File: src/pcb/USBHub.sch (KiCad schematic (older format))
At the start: 3 parts

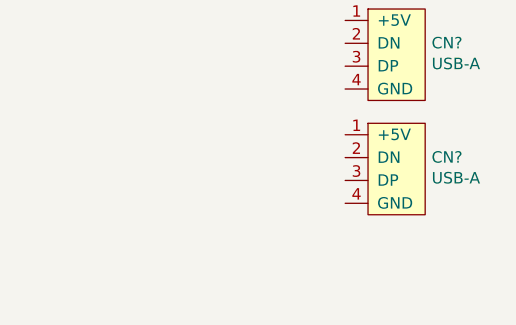
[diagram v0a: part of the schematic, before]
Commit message: added more connections, clarified schematic. Also added missing schematics
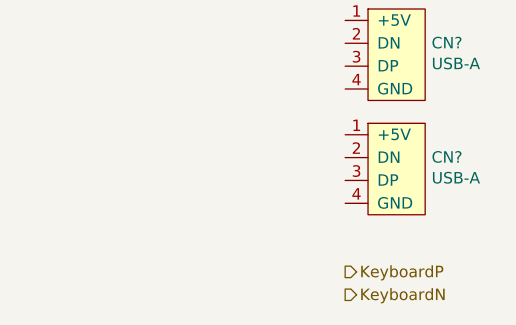
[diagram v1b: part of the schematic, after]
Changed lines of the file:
@@
 Text HLabel 7500 3500 2    50   Output ~ 0
 MCUUSBN
+Text HLabel 7500 5300 2    50   Output ~ 0
+KeyboardP
+Text HLabel 7500 5400 2    50   Output ~ 0
+KeyboardN
 $EndSCHEMATC

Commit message: tweaked libraries
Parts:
- CN? (x3): symbol Generic:USB-A -> generic:USB-A
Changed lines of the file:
@@
 $EndDescr
 $Comp
-L Generic:USB-A CN?
+L generic:USB-A CN?
 U 1 1 5C1FADC7
 P 7600 3800
@@
 $EndComp
 $Comp
-L Generic:USB-A CN?
+L generic:USB-A CN?
 U 1 1 5C1FAE2A
 P 7600 4300
@@
 $EndComp
 $Comp
-L Generic:USB-A CN?
+L generic:USB-A CN?
 U 1 1 5C1FAE58
 P 7600 4800
